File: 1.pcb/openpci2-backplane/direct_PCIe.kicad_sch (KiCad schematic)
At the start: 20 parts, among them J4 X3113WVS-64-9TV01, J5 AS0BC21-S30BM-7H, J6 X3113WVS-64-9TV01, J7 AS0BC21-S30BM-7H

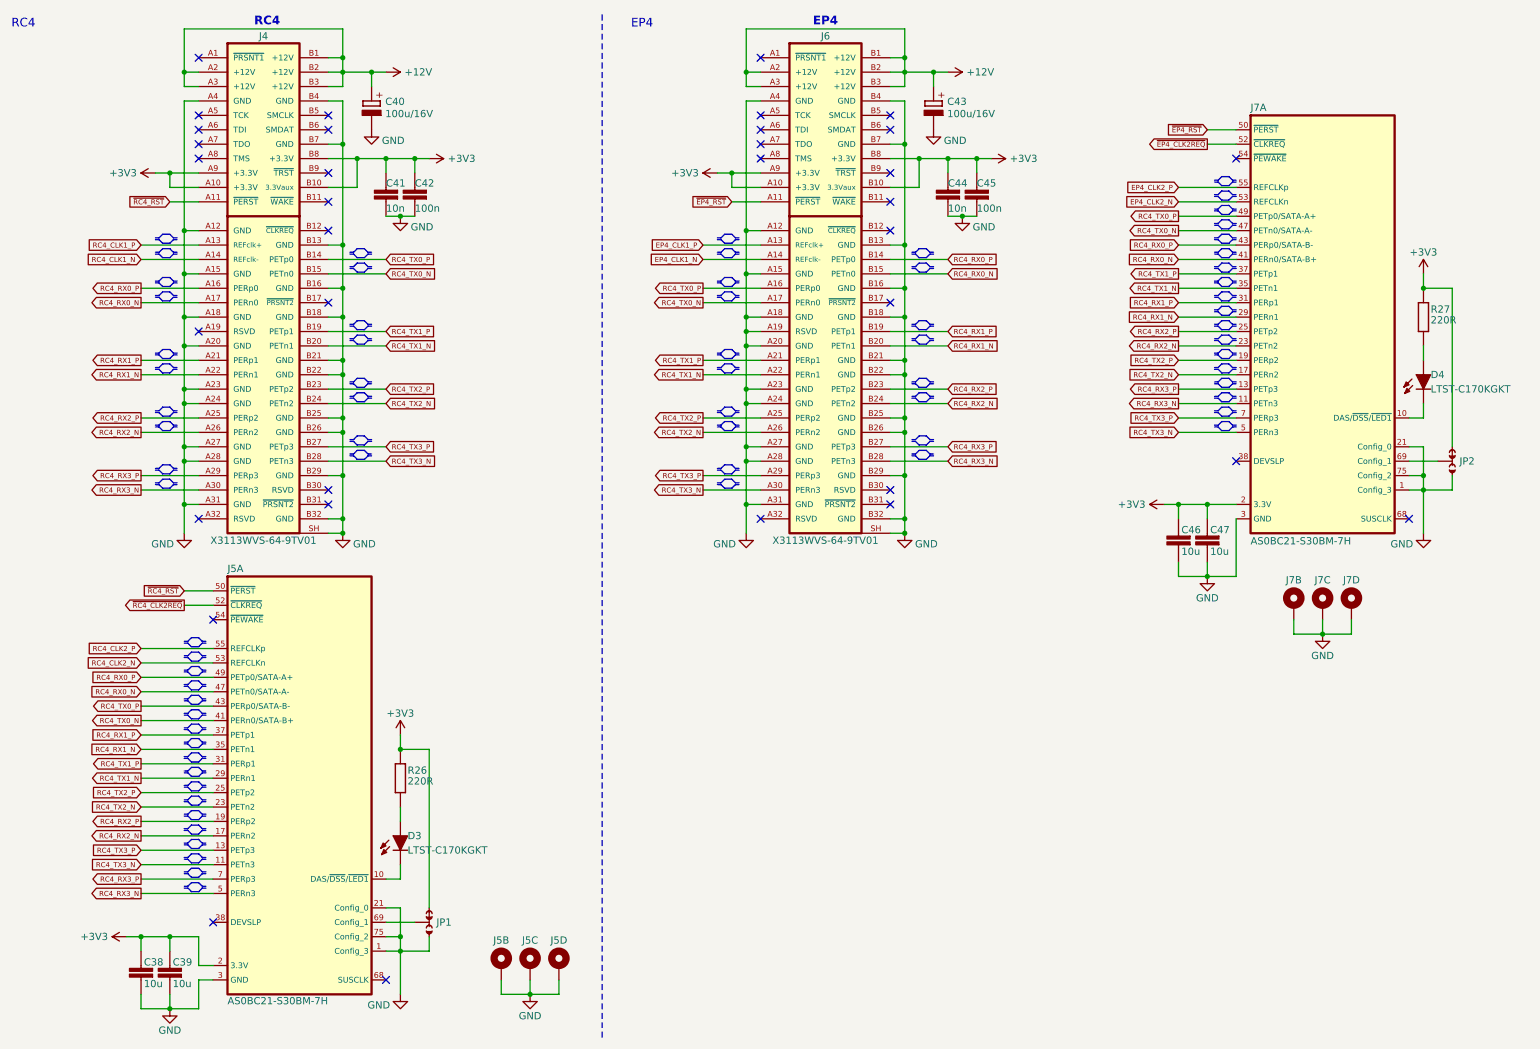
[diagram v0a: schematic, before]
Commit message: Rx/Tx lanes swap, RPi mounting holes
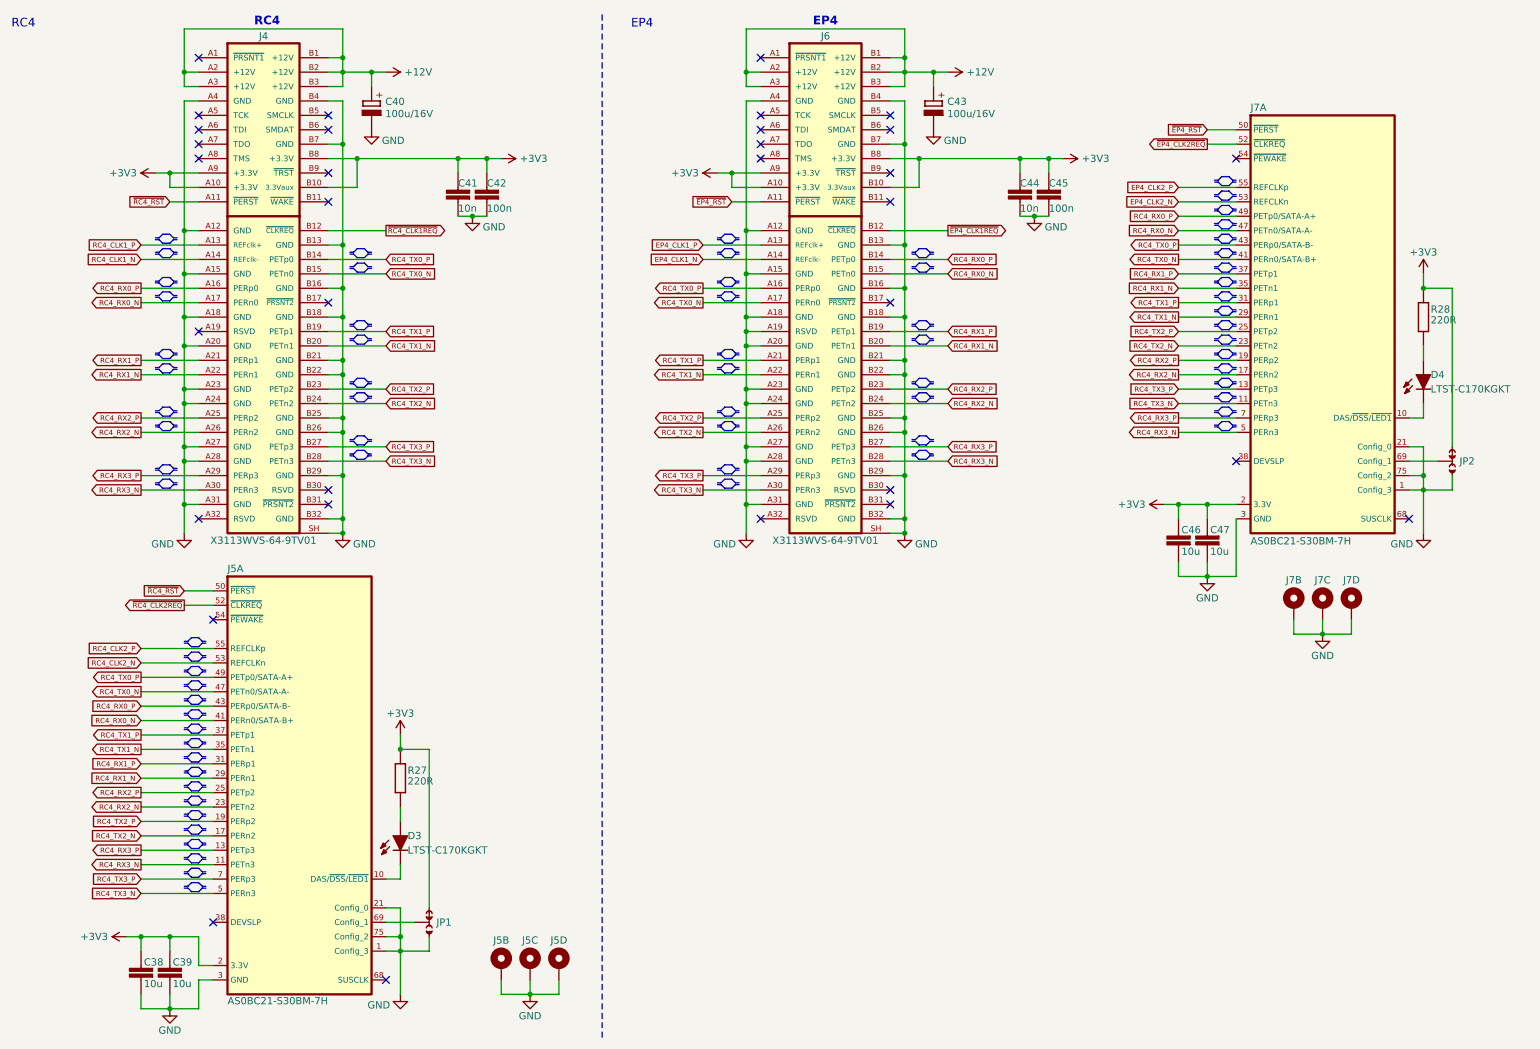
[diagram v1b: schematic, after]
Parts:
- renumbered R26 to R27, R27 to R28
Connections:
- net RC4_RX0_N: now also J5.41 (PERn0/SATA-B+), J7.47 (PETn0/SATA-A-); no longer J5.47 (PETn0/SATA-A-), J7.41 (PERn0/SATA-B+)
- net RC4_RX0_P: now also J5.43 (PERp0/SATA-B-), J7.49 (PETp0/SATA-A+); no longer J5.49 (PETp0/SATA-A+), J7.43 (PERp0/SATA-B-)
- net RC4_RX1_N: now also J5.29 (PERn1), J7.35 (PETn1); no longer J5.35 (PETn1), J7.29 (PERn1)
- net RC4_RX1_P: now also J5.31 (PERp1), J7.37 (PETp1); no longer J5.37 (PETp1), J7.31 (PERp1)
- net RC4_RX2_N: now also J5.23 (PETn2), J7.17 (PERn2); no longer J5.17 (PERn2), J7.23 (PETn2)
- net RC4_RX2_P: now also J5.25 (PETp2), J7.19 (PERp2); no longer J5.19 (PERp2), J7.25 (PETp2)
- net RC4_RX3_N: now also J5.11 (PETn3), J7.5 (PERn3); no longer J5.5 (PERn3), J7.11 (PETn3)
- net RC4_RX3_P: now also J5.13 (PETp3), J7.7 (PERp3); no longer J5.7 (PERp3), J7.13 (PETp3)
- net RC4_TX0_N: now also J5.47 (PETn0/SATA-A-), J7.41 (PERn0/SATA-B+); no longer J5.41 (PERn0/SATA-B+), J7.47 (PETn0/SATA-A-)
- net RC4_TX0_P: now also J5.49 (PETp0/SATA-A+), J7.43 (PERp0/SATA-B-); no longer J5.43 (PERp0/SATA-B-), J7.49 (PETp0/SATA-A+)
- net RC4_TX1_N: now also J5.35 (PETn1), J7.29 (PERn1); no longer J5.29 (PERn1), J7.35 (PETn1)
- net RC4_TX1_P: now also J5.37 (PETp1), J7.31 (PERp1); no longer J5.31 (PERp1), J7.37 (PETp1)
- net RC4_TX2_N: now also J5.17 (PERn2), J7.23 (PETn2); no longer J5.23 (PETn2), J7.17 (PERn2)
- net RC4_TX2_P: now also J5.19 (PERp2), J7.25 (PETp2); no longer J5.25 (PETp2), J7.19 (PERp2)
- net RC4_TX3_N: now also J5.5 (PERn3), J7.11 (PETn3); no longer J5.11 (PETn3), J7.5 (PERn3)
- net RC4_TX3_P: now also J5.7 (PERp3), J7.13 (PETp3); no longer J5.13 (PETp3), J7.7 (PERp3)
- net ~{EP4_CLK1REQ}: now reaches J6.B12 (~{CLKREQ})
- net ~{RC4_CLK1REQ}: now reaches J4.B12 (~{CLKREQ})
- no-connect marks 35 -> 33
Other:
- moved on the sheet: C41, C42, C44, C45

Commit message: Rx/Tx lanes swap
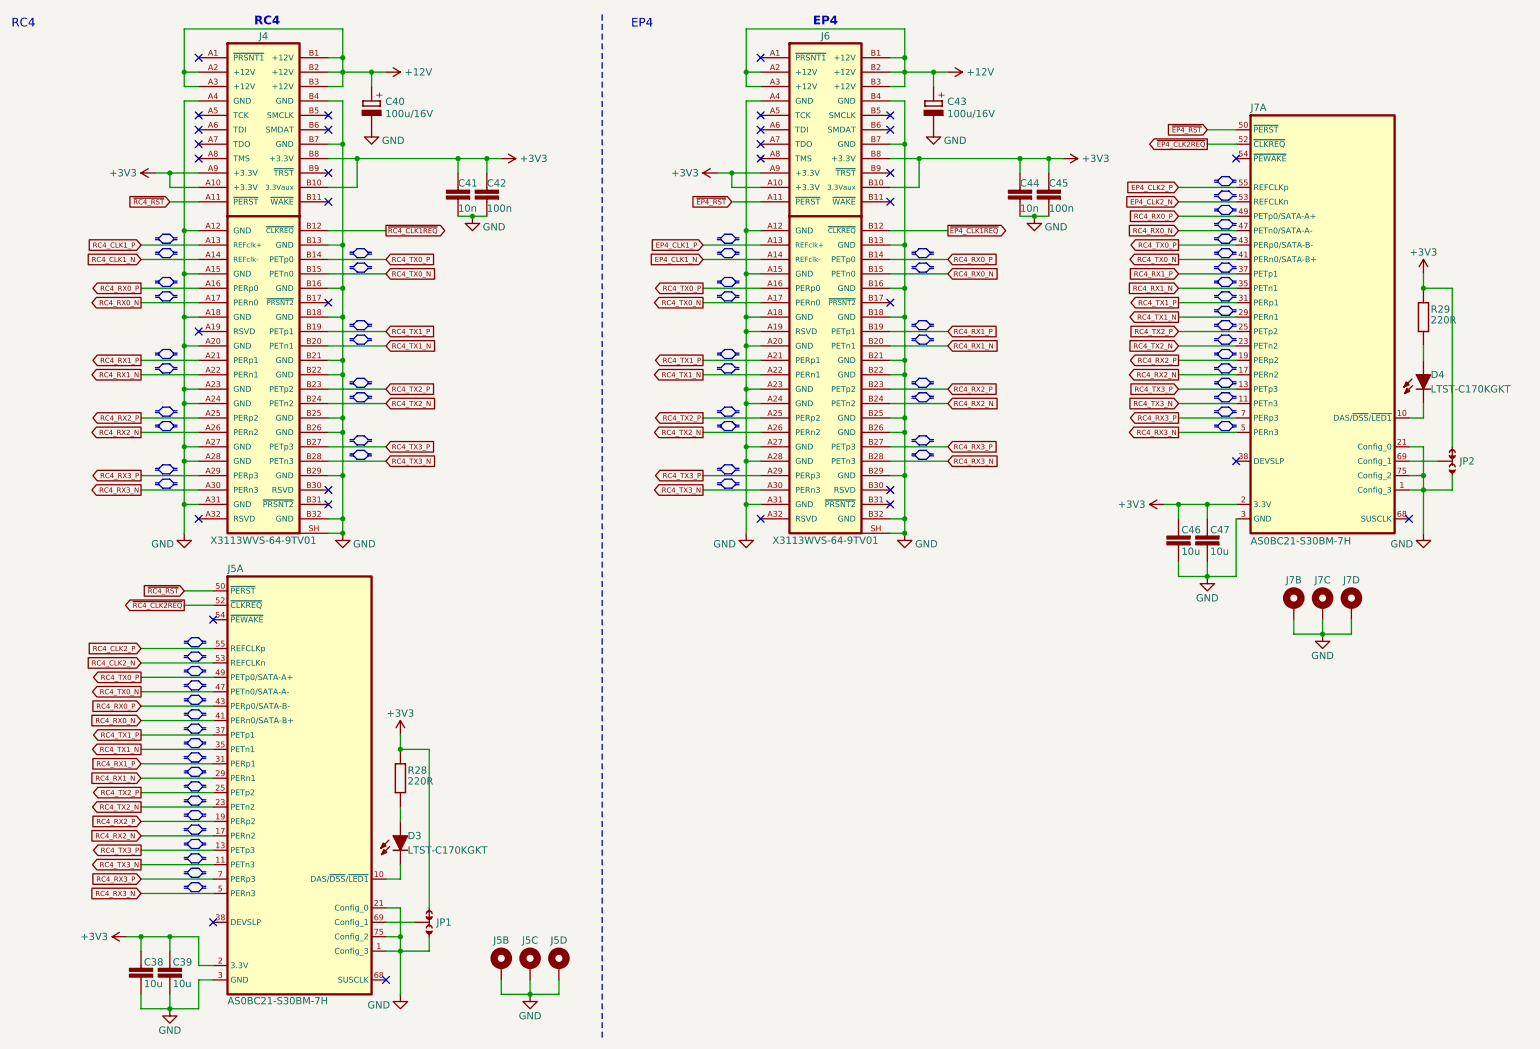
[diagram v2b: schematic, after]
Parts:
- renumbered R27 to R28, R28 to R29
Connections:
- net RC4_RX2_N: now also J5.17 (PERn2); no longer J5.23 (PETn2)
- net RC4_RX2_P: now also J5.19 (PERp2); no longer J5.25 (PETp2)
- net RC4_RX3_N: now also J5.5 (PERn3); no longer J5.11 (PETn3)
- net RC4_RX3_P: now also J5.7 (PERp3); no longer J5.13 (PETp3)
- net RC4_TX2_N: now also J5.23 (PETn2); no longer J5.17 (PERn2)
- net RC4_TX2_P: now also J5.25 (PETp2); no longer J5.19 (PERp2)
- net RC4_TX3_N: now also J5.11 (PETn3); no longer J5.5 (PERn3)
- net RC4_TX3_P: now also J5.13 (PETp3); no longer J5.7 (PERp3)

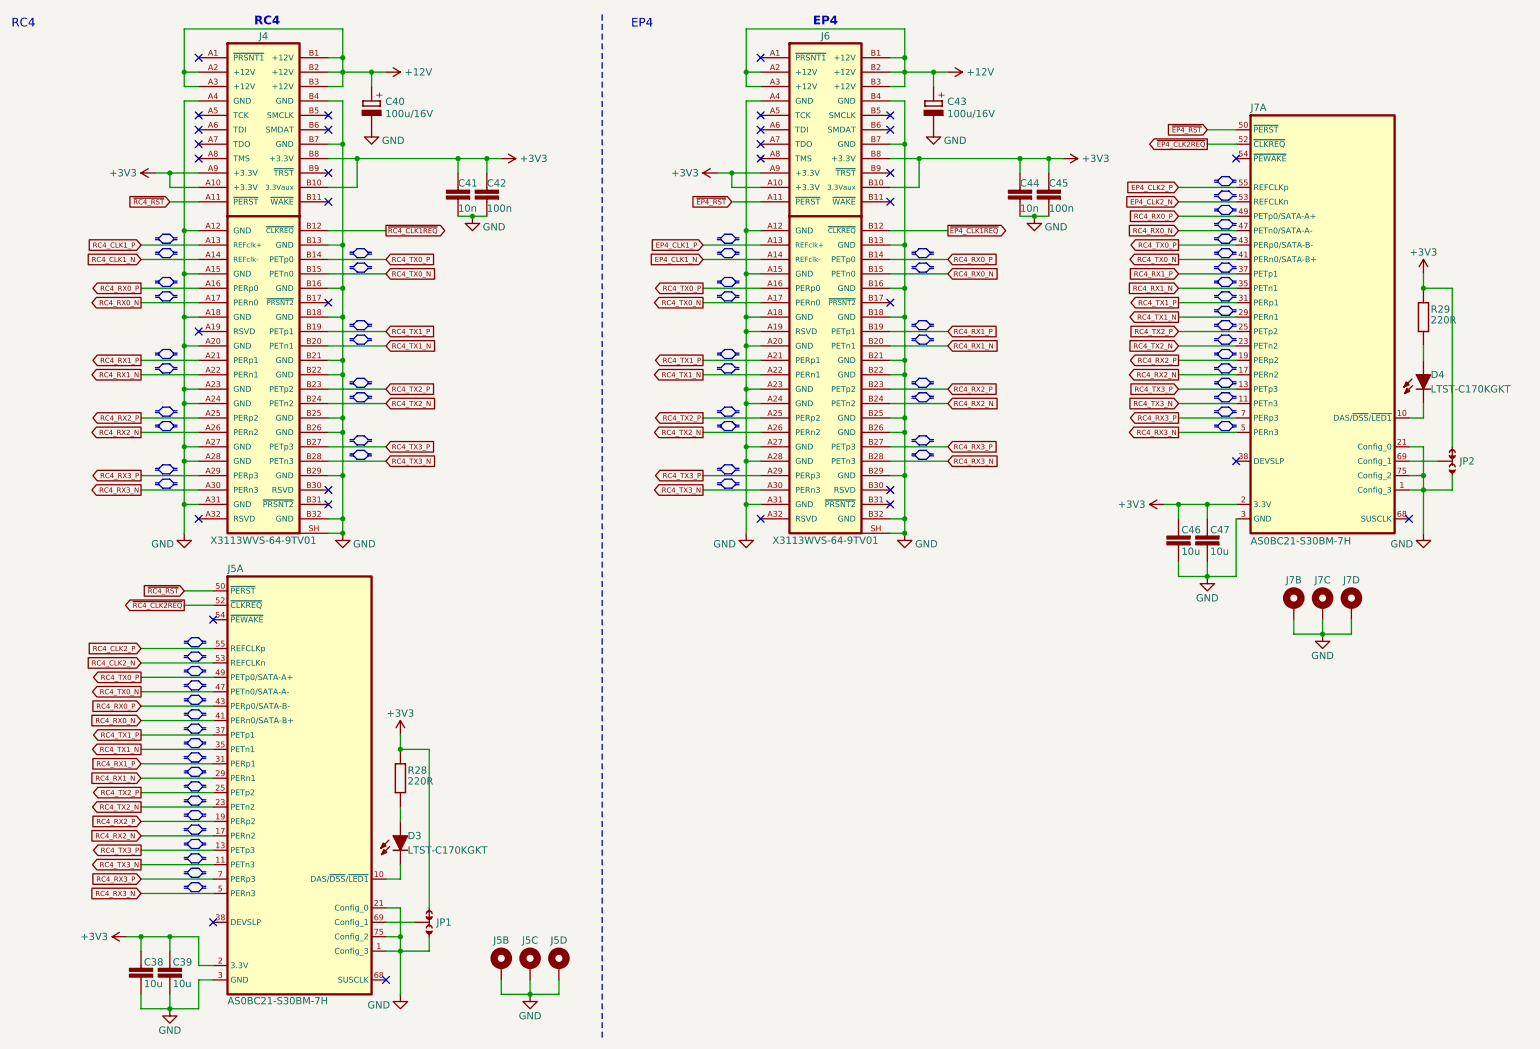
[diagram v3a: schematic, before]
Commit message: U5 PD capacitor added, BOM updated
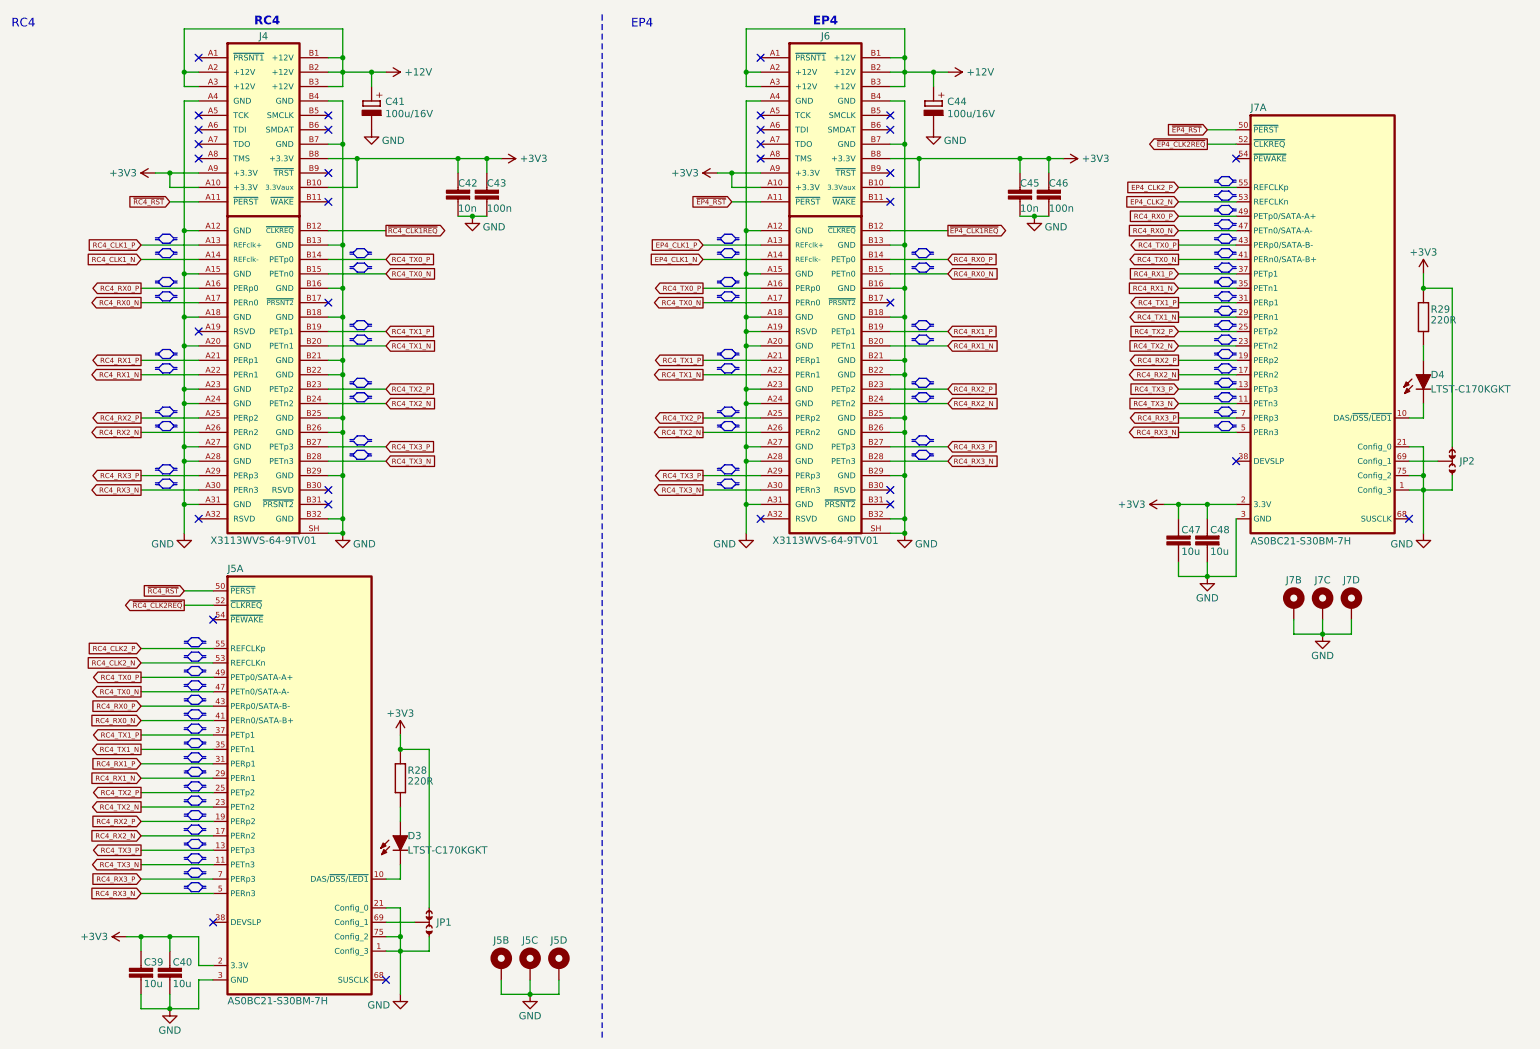
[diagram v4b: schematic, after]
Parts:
- renumbered C38 to C39, C39 to C40, C40 to C41, C41 to C42, C42 to C43, C43 to C44, C44 to C45, C45 to C46, C46 to C47, C47 to C48

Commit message: Schematic complete and ready for PCB layout
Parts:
- C39, C40, C47, C48: Mouser 187-CL21A106KPFNNNE -> (none); TME CL21A106KPFNNNE -> (none); Voltage (none) -> 10V
- C41, C44: value 100u/16V -> 100u; Mouser 667-EEE-1CA101WAP -> (none); TME EEE1CA101WAP -> (none); Voltage (none) -> 16V
- C42, C45: footprint PCM_EEZ_passives:C_0603_1608Metric -> PCM_EEZ_passives:C_0402_1005Metric; DigiKey 1276-1000-1-ND -> 490-1313-1-ND; Mouser 187-CL10B104KB8NNNC -> (none); TME CL10B104KB8NNNC -> (none); Voltage (none) -> 16V
- C43, C46: DigiKey 1276-1000-1-ND -> 490-6321-1-ND; Mouser 187-CL10B104KB8NNNC -> (none); TME CL10B104KB8NNNC -> (none); Voltage (none) -> 10V
- D3, D4: Mouser 859-LTST-C170KGKT -> (none); TME LTST-C170KGKT -> (none)
- J4, J5, J6, J7: DigiKey - -> (none); Mouser - -> (none); TME - -> (none)
- R28, R29: DigiKey 490-5178-1-ND -> 311-220GRCT-ND; LCSC C85813 -> (none); Mouser 81-BLM15AG221SN1D -> (none); TME BLM15AG221SN1Dž -> (none)
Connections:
- net GND: no longer J6.A19 (RSVD)
- no-connect marks 33 -> 34
